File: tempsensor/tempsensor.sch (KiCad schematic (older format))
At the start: 68 parts, among them J1 USB_B_Micro, Q1 BC817, Q2 BC817, Q3 BC817, SW1 SW_DIP_x06, SW2 PW_OFF, SW3 PW_ON, U1 PCF8574, U2 ESP-12F, U3 24C16, U4 MCP73831-2-OT, U5 MCP9844, U6 MAX17620

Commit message: Added some footprints to tempsensor.
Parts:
- C1, C2, C3, C6, C8, C9: footprint (none) -> Capacitor_SMD:C_0603_1608Metric
- TP1, TP2: footprint (none) -> TestPoint:TestPoint_Pad_4.0x4.0mm
- TP10, TP11, TP12, TP13, TP14, TP15, TP16, TP3, TP4, TP5, TP6, TP7, TP8, TP9: footprint (none) -> TestPoint:TestPoint_Pad_D1.0mm
- U3: footprint (none) -> Package_DIP:SMDIP-8_W7.62mm
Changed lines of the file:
@@
 F 0 "C6" H 4715 5096 50  0000 L CNN
 F 1 "100n" H 4715 5005 50  0000 L CNN
-F 2 "" H 4638 4900 50  0001 C CNN
+F 2 "Capacitor_SMD:C_0603_1608Metric" H 4638 4900 50  0001 C CNN
 F 3 "~" H 4600 5050 50  0001 C CNN
 	1    4600 5050
@@
 F 0 "TP2" H 6208 6468 50  0000 L CNN
 F 1 "TestPoint" H 6208 6377 50  0000 L CNN
-F 2 "" H 6350 6350 50  0001 C CNN
+F 2 "TestPoint:TestPoint_Pad_4.0x4.0mm" H 6350 6350 50  0001 C CNN
 F 3 "~" H 6350 6350 50  0001 C CNN
 	1    6150 6350
@@
 F 0 "C1" H 1515 4796 50  0000 L CNN
 F 1 "10n" H 1515 4705 50  0000 L CNN
-F 2 "" H 1438 4600 50  0001 C CNN
+F 2 "Capacitor_SMD:C_0603_1608Metric" H 1438 4600 50  0001 C CNN
 F 3 "~" H 1400 4750 50  0001 C CNN
 	1    1400 4750
@@
 F 0 "U3" H 2500 6800 50  0000 C CNN
 F 1 "24C16" H 3000 6800 50  0000 C CNN
-F 2 "" H 2750 6500 50  0001 C CNN
+F 2 "Package_DIP:SMDIP-8_W7.62mm" H 2750 6500 50  0001 C CNN
 F 3 "https://www.onsemi.com/pub/Collateral/CAT24C128-D.PDF" H 2750 6500 50  0001 C CNN
 	1    2750 6500
@@
 F 0 "C3" V 2298 6050 50  0000 C CNN
 F 1 "100n" V 2389 6050 50  0000 C CNN
-F 2 "" H 2588 5900 50  0001 C CNN
+F 2 "Capacitor_SMD:C_0603_1608Metric" H 2588 5900 50  0001 C CNN
 F 3 "~" H 2550 6050 50  0001 C CNN
 	1    2550 6050
@@
 F 0 "C8" V 5348 3750 50  0000 C CNN
 F 1 "10n" V 5439 3750 50  0000 C CNN
-F 2 "" H 5638 3600 50  0001 C CNN
+F 2 "Capacitor_SMD:C_0603_1608Metric" H 5638 3600 50  0001 C CNN
 F 3 "~" H 5600 3750 50  0001 C CNN
 	1    5600 3750
@@
 F 0 "TP10" V 9504 3738 50  0000 L CNN
 F 1 "SCL" V 9595 3738 50  0000 L CNN
-F 2 "" H 9750 3550 50  0001 C CNN
+F 2 "TestPoint:TestPoint_Pad_D1.0mm" H 9750 3550 50  0001 C CNN
 F 3 "~" H 9750 3550 50  0001 C CNN
 	1    9550 3550
@@
 F 0 "TP11" V 9504 3938 50  0000 L CNN
 F 1 "SDA" V 9595 3938 50  0000 L CNN
-F 2 "" H 9750 3750 50  0001 C CNN
+F 2 "TestPoint:TestPoint_Pad_D1.0mm" H 9750 3750 50  0001 C CNN
 F 3 "~" H 9750 3750 50  0001 C CNN
 	1    9550 3750
@@
 F 0 "TP12" V 9504 4138 50  0000 L CNN
 F 1 "3V3" V 9595 4138 50  0000 L CNN
-F 2 "" H 9750 3950 50  0001 C CNN
+F 2 "TestPoint:TestPoint_Pad_D1.0mm" H 9750 3950 50  0001 C CNN
 F 3 "~" H 9750 3950 50  0001 C CNN
 	1    9550 3950
@@
 F 0 "TP13" V 9498 4338 50  0000 L CNN
 F 1 "~UVSLO" V 9596 4338 50  0000 L CNN
-F 2 "" H 9750 4150 50  0001 C CNN
+F 2 "TestPoint:TestPoint_Pad_D1.0mm" H 9750 4150 50  0001 C CNN
 F 3 "~" H 9750 4150 50  0001 C CNN
 	1    9550 4150
@@
 F 0 "TP14" V 9504 4538 50  0000 L CNN
 F 1 "VDC" V 9595 4538 50  0000 L CNN
-F 2 "" H 9750 4350 50  0001 C CNN
+F 2 "TestPoint:TestPoint_Pad_D1.0mm" H 9750 4350 50  0001 C CNN
 F 3 "~" H 9750 4350 50  0001 C CNN
 	1    9550 4350
@@
 F 0 "TP3" V 8554 3738 50  0000 L CNN
 F 1 "VBUS" V 8645 3738 50  0000 L CNN
-F 2 "" H 8800 3550 50  0001 C CNN
+F 2 "TestPoint:TestPoint_Pad_D1.0mm" H 8800 3550 50  0001 C CNN
 F 3 "~" H 8800 3550 50  0001 C CNN
 	1    8600 3550
@@
 F 0 "TP4" V 8554 3938 50  0000 L CNN
 F 1 "GND" V 8645 3938 50  0000 L CNN
-F 2 "" H 8800 3750 50  0001 C CNN
+F 2 "TestPoint:TestPoint_Pad_D1.0mm" H 8800 3750 50  0001 C CNN
 F 3 "~" H 8800 3750 50  0001 C CNN
 	1    8600 3750
@@
 F 0 "TP5" V 8554 4138 50  0000 L CNN
 F 1 "RXD" V 8645 4138 50  0000 L CNN
-F 2 "" H 8800 3950 50  0001 C CNN
+F 2 "TestPoint:TestPoint_Pad_D1.0mm" H 8800 3950 50  0001 C CNN
 F 3 "~" H 8800 3950 50  0001 C CNN
 	1    8600 3950
@@
 F 0 "TP7" V 8554 4538 50  0000 L CNN
 F 1 "DTR" V 8645 4538 50  0000 L CNN
-F 2 "" H 8800 4350 50  0001 C CNN
+F 2 "TestPoint:TestPoint_Pad_D1.0mm" H 8800 4350 50  0001 C CNN
 F 3 "~" H 8800 4350 50  0001 C CNN
 	1    8600 4350
@@
 F 0 "TP8" V 8554 4738 50  0000 L CNN
 F 1 "RTS" V 8645 4738 50  0000 L CNN
-F 2 "" H 8800 4550 50  0001 C CNN
+F 2 "TestPoint:TestPoint_Pad_D1.0mm" H 8800 4550 50  0001 C CNN
 F 3 "~" H 8800 4550 50  0001 C CNN
 	1    8600 4550
@@
 F 0 "TP15" V 9504 4738 50  0000 L CNN
 F 1 "BAT+" V 9595 4738 50  0000 L CNN
-F 2 "" H 9750 4550 50  0001 C CNN
+F 2 "TestPoint:TestPoint_Pad_D1.0mm" H 9750 4550 50  0001 C CNN
 F 3 "~" H 9750 4550 50  0001 C CNN
 	1    9550 4550
@@
 F 0 "C2" V 1548 1000 50  0000 C CNN
 F 1 "100n" V 1639 1000 50  0000 C CNN
-F 2 "" H 1838 850 50  0001 C CNN
+F 2 "Capacitor_SMD:C_0603_1608Metric" H 1838 850 50  0001 C CNN
 F 3 "~" H 1800 1000 50  0001 C CNN
 	1    1800 1000
@@
 F 0 "TP1" H 6092 5976 50  0000 R CNN
 F 1 "TestPoint" H 6092 6067 50  0000 R CNN
-F 2 "" H 6350 5950 50  0001 C CNN
+F 2 "TestPoint:TestPoint_Pad_4.0x4.0mm" H 6350 5950 50  0001 C CNN
 F 3 "~" H 6350 5950 50  0001 C CNN
 	1    6150 5950
@@
 F 0 "TP6" V 8554 4338 50  0000 L CNN
 F 1 "TXD" V 8645 4338 50  0000 L CNN
-F 2 "" H 8800 4150 50  0001 C CNN
+F 2 "TestPoint:TestPoint_Pad_D1.0mm" H 8800 4150 50  0001 C CNN
 F 3 "~" H 8800 4150 50  0001 C CNN
 	1    8600 4150
@@
 F 0 "C9" V 6398 4400 50  0000 C CNN
 F 1 "1u" V 6489 4400 50  0000 C CNN
-F 2 "" H 6688 4250 50  0001 C CNN
+F 2 "Capacitor_SMD:C_0603_1608Metric" H 6688 4250 50  0001 C CNN
 F 3 "~" H 6650 4400 50  0001 C CNN
 	1    6650 4400
@@
 F 0 "TP9" V 8554 4938 50  0000 L CNN
 F 1 "~RST" V 8645 4938 50  0000 L CNN
-F 2 "" H 8800 4750 50  0001 C CNN
+F 2 "TestPoint:TestPoint_Pad_D1.0mm" H 8800 4750 50  0001 C CNN
 F 3 "~" H 8800 4750 50  0001 C CNN
 	1    8600 4750
@@
 F 0 "TP16" V 9504 4938 50  0000 L CNN
 F 1 "TMP" V 9595 4938 50  0000 L CNN
-F 2 "" H 9750 4750 50  0001 C CNN
+F 2 "TestPoint:TestPoint_Pad_D1.0mm" H 9750 4750 50  0001 C CNN
 F 3 "~" H 9750 4750 50  0001 C CNN
 	1    9550 4750

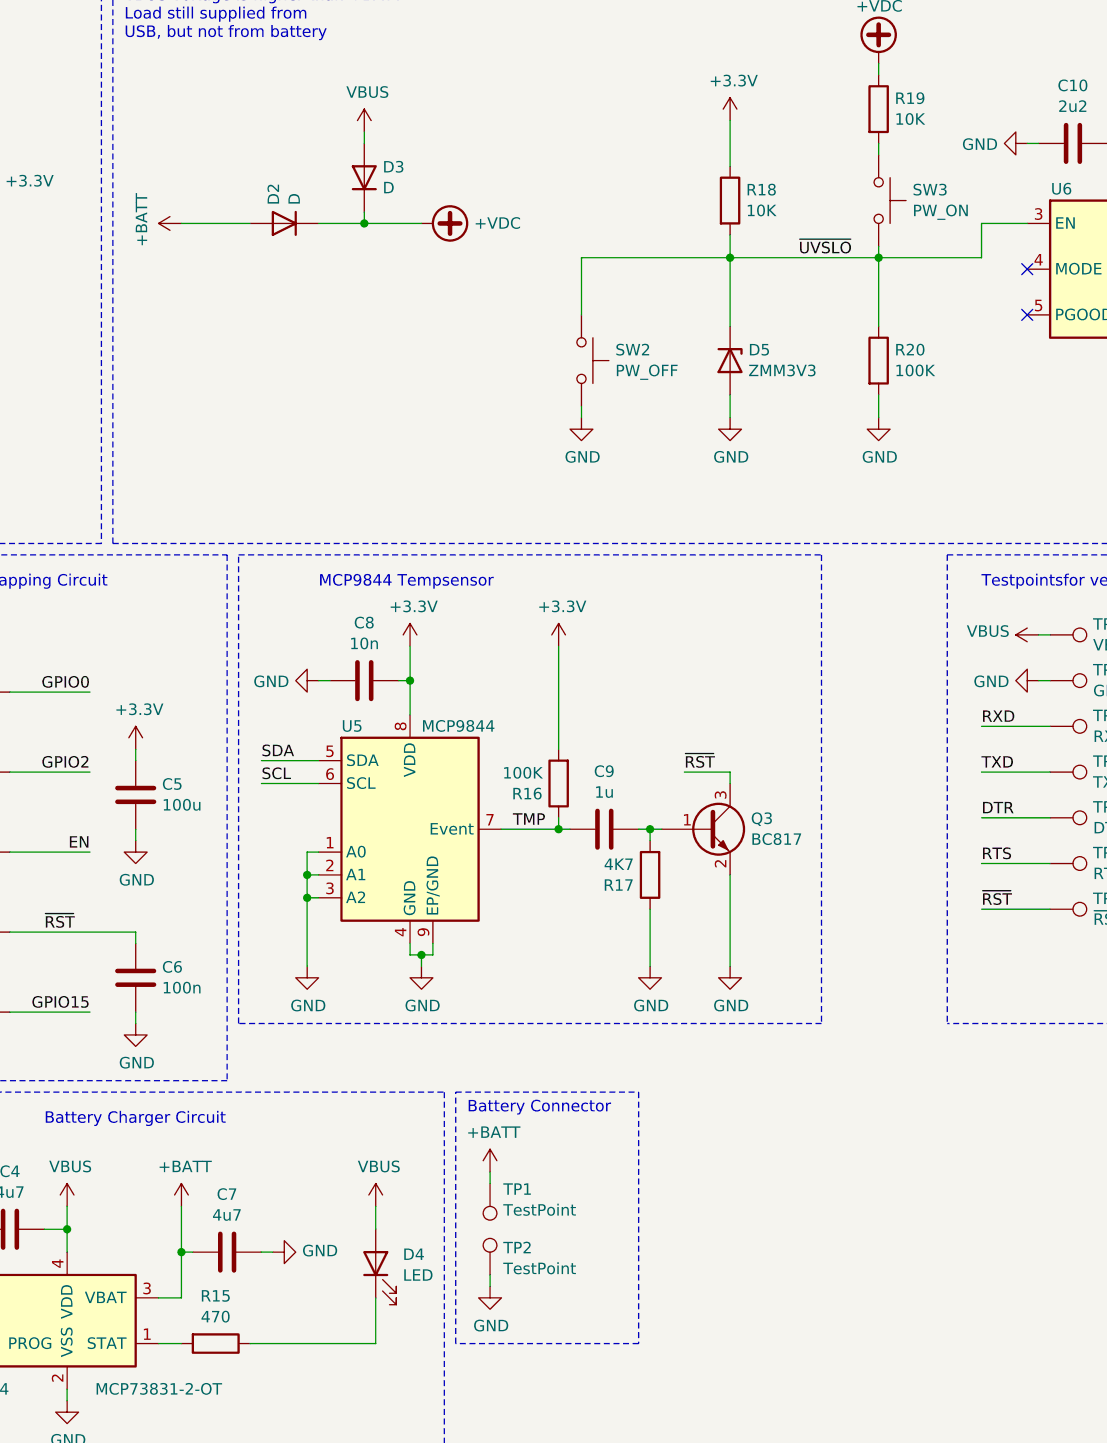
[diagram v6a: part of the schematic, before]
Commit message: Tempsensor finished adding footprints
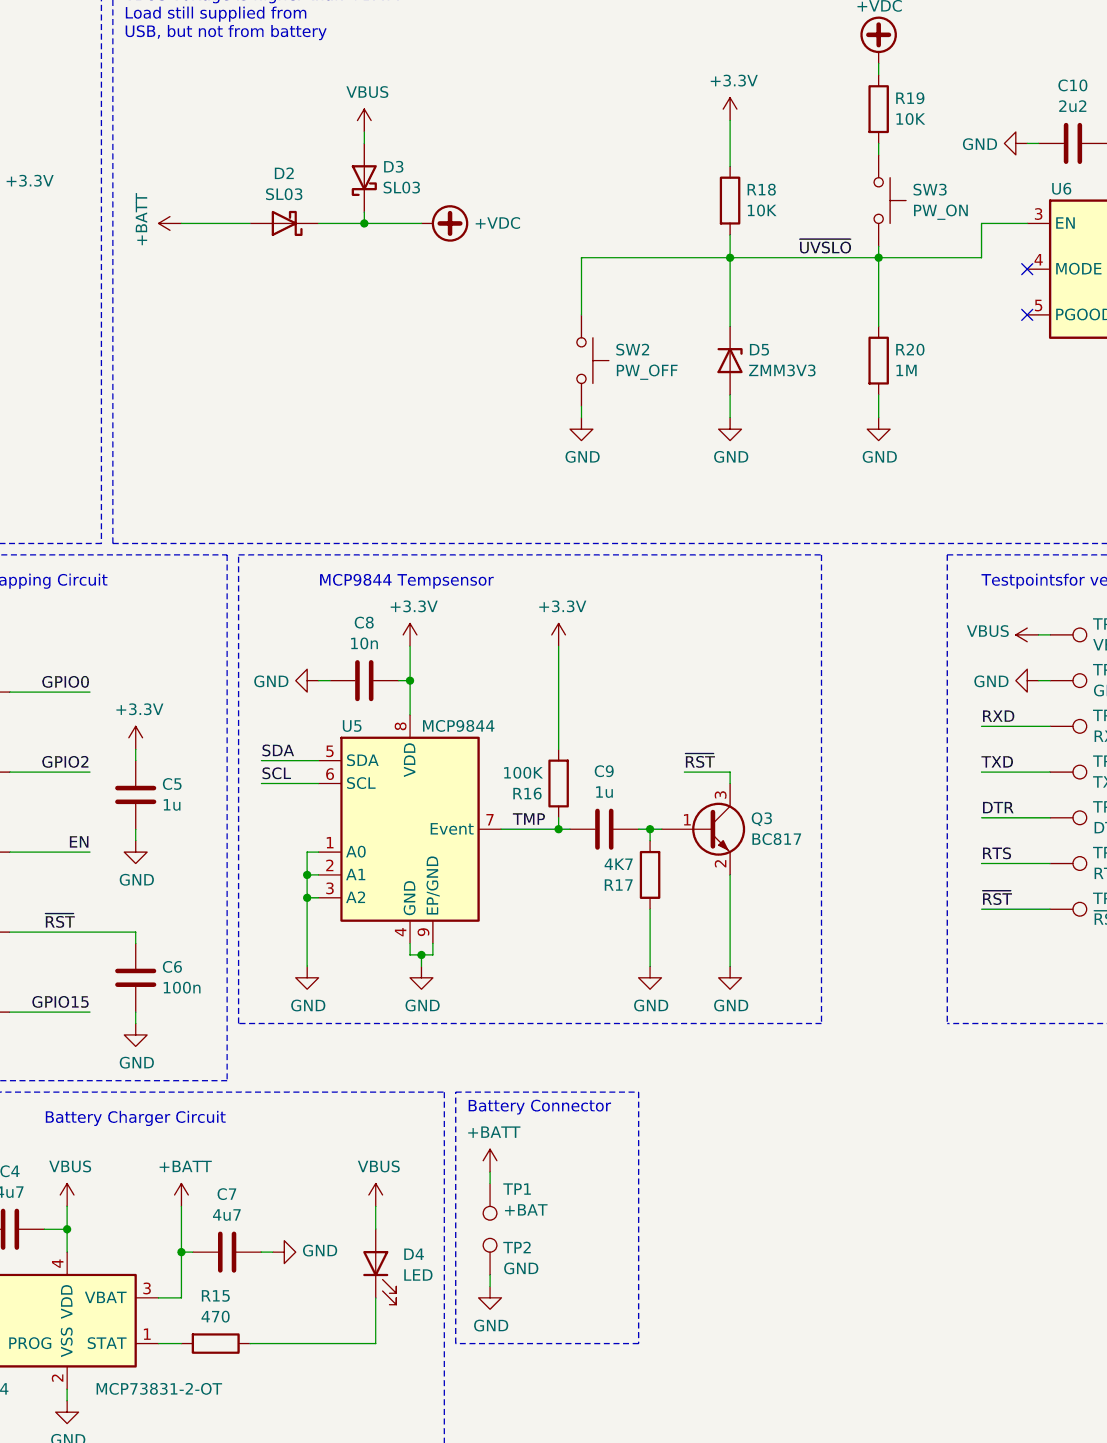
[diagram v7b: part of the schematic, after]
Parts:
- removed D2, D3: D, symbol Device:D
- added D2, D3: SL03, Diode_SMD:D_SMF, symbol Device:D_Schottky
- C10: footprint (none) -> Capacitor_SMD:C_0603_1608Metric
- C11, C4, C7: footprint (none) -> Capacitor_SMD:C_0805_2012Metric
- C5: value 100u -> 1u; footprint (none) -> Capacitor_SMD:C_0603_1608Metric
- D5: footprint (none) -> Diode_SMD:D_MiniMELF
- R20: value 100K -> 1M
- SW1: footprint (none) -> Button_Switch_SMD:SW_DIP_SPSTx06_Slide_Omron_A6S-610x_W8.9mm_P2.54mm
- SW2, SW3: footprint (none) -> Button_Switch_THT:SW_PUSH_6mm_H5mm
- TP1: value TestPoint -> +BAT
- TP2: value TestPoint -> GND
- U3: footprint Package_DIP:SMDIP-8_W7.62mm -> Package_SO:SOIC-8_3.9x4.9mm_P1.27mm
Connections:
- net +BATT: now also D2.2 (A)
- net +VDC: now also D2.1 (K), D3.1 (K)
- net VBUS: now also D3.2 (A)
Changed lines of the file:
@@
 F 0 "C4" V 3798 6150 50  0000 C CNN
 F 1 "4u7" V 3889 6150 50  0000 C CNN
-F 2 "" H 4088 6000 50  0001 C CNN
+F 2 "Capacitor_SMD:C_0805_2012Metric" H 4088 6000 50  0001 C CNN
 F 3 "~" H 4050 6150 50  0001 C CNN
 	1    4050 6150
@@
 F 0 "C7" V 4748 6250 50  0000 C CNN
 F 1 "4u7" V 4839 6250 50  0000 C CNN
-F 2 "" H 5038 6100 50  0001 C CNN
+F 2 "Capacitor_SMD:C_0805_2012Metric" H 5038 6100 50  0001 C CNN
 F 3 "~" H 5000 6250 50  0001 C CNN
 	1    5000 6250
@@
 F 0 "C10" V 8448 1400 50  0000 C CNN
 F 1 "2u2" V 8539 1400 50  0000 C CNN
-F 2 "" H 8738 1250 50  0001 C CNN
+F 2 "Capacitor_SMD:C_0603_1608Metric" H 8738 1250 50  0001 C CNN
 F 3 "~" H 8700 1400 50  0001 C CNN
 	1    8700 1400
@@
 F 0 "C11" H 10865 2146 50  0000 L CNN
 F 1 "10u" H 10865 2055 50  0000 L CNN
-F 2 "" H 10788 1950 50  0001 C CNN
+F 2 "Capacitor_SMD:C_0805_2012Metric" H 10788 1950 50  0001 C CNN
 F 3 "~" H 10750 2100 50  0001 C CNN
 	1    10750 2100
@@
 P 4600 4250
 F 0 "C5" H 4715 4296 50  0000 L CNN
-F 1 "100u" H 4715 4205 50  0000 L CNN
-F 2 "" H 4638 4100 50  0001 C CNN
+F 1 "1u" H 4715 4205 50  0000 L CNN
+F 2 "Capacitor_SMD:C_0603_1608Metric" H 4638 4100 50  0001 C CNN
 F 3 "~" H 4600 4250 50  0001 C CNN
 	1    4600 4250
@@
 Wire Notes Line
 	3550 5500 3550 3200
-$Comp
-L Device:D D3
-U 1 1 5E75AE77
-P 5600 1550
-F 0 "D3" V 5646 1470 50  0000 R CNN
-F 1 "D" V 5555 1470 50  0000 R CNN
-F 2 "" H 5600 1550 50  0001 C CNN
-F 3 "~" H 5600 1550 50  0001 C CNN
-	1    5600 1550
-	0    -1   -1   0
-$EndComp
 Wire Wire Line
 	5600 1700 5600 1750
@@
 P 6150 6350
 F 0 "TP2" H 6208 6468 50  0000 L CNN
-F 1 "TestPoint" H 6208 6377 50  0000 L CNN
+F 1 "GND" H 6208 6377 50  0000 L CNN
 F 2 "TestPoint:TestPoint_Pad_4.0x4.0mm" H 6350 6350 50  0001 C CNN
 F 3 "~" H 6350 6350 50  0001 C CNN
@@
 F 0 "U3" H 2500 6800 50  0000 C CNN
 F 1 "24C16" H 3000 6800 50  0000 C CNN
-F 2 "Package_DIP:SMDIP-8_W7.62mm" H 2750 6500 50  0001 C CNN
+F 2 "Package_SO:SOIC-8_3.9x4.9mm_P1.27mm" H 2750 6500 50  0001 C CNN
 F 3 "https://www.onsemi.com/pub/Collateral/CAT24C128-D.PDF" H 2750 6500 50  0001 C CNN
 	1    2750 6500
@@
 P 7850 2350
 F 0 "R20" H 7920 2396 50  0000 L CNN
-F 1 "100K" H 7920 2305 50  0000 L CNN
+F 1 "1M" H 7920 2305 50  0000 L CNN
 F 2 "Resistor_SMD:R_0603_1608Metric" V 7780 2350 50  0001 C CNN
 F 3 "~" H 7850 2350 50  0001 C CNN
@@
 F 0 "SW2" V 6504 2498 50  0000 L CNN
 F 1 "PW_OFF" V 6595 2498 50  0000 L CNN
-F 2 "" H 6550 2550 50  0001 C CNN
+F 2 "Button_Switch_THT:SW_PUSH_6mm_H5mm" H 6550 2550 50  0001 C CNN
 F 3 "~" H 6550 2550 50  0001 C CNN
 	1    6550 2350
@@
 	8300 1750 8500 1750
 Connection ~ 7850 1900
-$Comp
-L Device:D D2
-U 1 1 5EC8A63C
-P 5250 1750
-F 0 "D2" V 5296 1670 50  0000 R CNN
-F 1 "D" V 5205 1670 50  0000 R CNN
-F 2 "" H 5250 1750 50  0001 C CNN
-F 3 "~" H 5250 1750 50  0001 C CNN
-	1    5250 1750
-	-1   0    0    1
-$EndComp
 Wire Wire Line
 	4800 1750 5100 1750
@@
 F 0 "D5" V 7154 2430 50  0000 L CNN
 F 1 "ZMM3V3" V 7245 2430 50  0000 L CNN
-F 2 "" H 7200 2350 50  0001 C CNN
+F 2 "Diode_SMD:D_MiniMELF" H 7200 2350 50  0001 C CNN
 F 3 "~" H 7200 2350 50  0001 C CNN
 	1    7200 2350
@@
 F 0 "SW1" V 2704 2930 50  0000 L CNN
 F 1 "SW_DIP_x06" V 2795 2930 50  0000 L CNN
-F 2 "" H 2750 2500 50  0001 C CNN
+F 2 "Button_Switch_SMD:SW_DIP_SPSTx06_Slide_Omron_A6S-610x_W8.9mm_P2.54mm" H 2750 2500 50  0001 C CNN
 F 3 "~" H 2750 2500 50  0001 C CNN
 	1    2750 2500
@@
 P 6150 5950
 F 0 "TP1" H 6092 5976 50  0000 R CNN
-F 1 "TestPoint" H 6092 6067 50  0000 R CNN
+F 1 "+BAT" H 6092 6067 50  0000 R CNN
 F 2 "TestPoint:TestPoint_Pad_4.0x4.0mm" H 6350 5950 50  0001 C CNN
 F 3 "~" H 6350 5950 50  0001 C CNN
@@
 F 0 "SW3" V 7804 1798 50  0000 L CNN
 F 1 "PW_ON" V 7895 1798 50  0000 L CNN
-F 2 "" H 7850 1850 50  0001 C CNN
+F 2 "Button_Switch_THT:SW_PUSH_6mm_H5mm" H 7850 1850 50  0001 C CNN
 F 3 "~" H 7850 1850 50  0001 C CNN
 	1    7850 1650
@@
 Wire Wire Line
 	9250 4750 9550 4750
+$Comp
+L Device:D_Schottky D2
+U 1 1 5F01FFB4
+P 5250 1750
+F 0 "D2" H 5250 1533 50  0000 C CNN
+F 1 "SL03" H 5250 1624 50  0000 C CNN
+F 2 "Diode_SMD:D_SMF" H 5250 1750 50  0001 C CNN
+F 3 "~" H 5250 1750 50  0001 C CNN
+	1    5250 1750
+	-1   0    0    1
+$EndComp
+$Comp
+L Device:D_Schottky D3
+U 1 1 5F0204FB
+P 5600 1550
+F 0 "D3" V 5646 1470 50  0000 R CNN
+F 1 "SL03" V 5555 1470 50  0000 R CNN
+F 2 "Diode_SMD:D_SMF" H 5600 1550 50  0001 C CNN
+F 3 "~" H 5600 1550 50  0001 C CNN
+	1    5600 1550
+	0    -1   -1   0
+$EndComp
 $EndSCHEMATC
